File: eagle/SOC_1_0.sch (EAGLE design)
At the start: 16 parts, among them X1 A, X2 B, X3 X, X4 Y

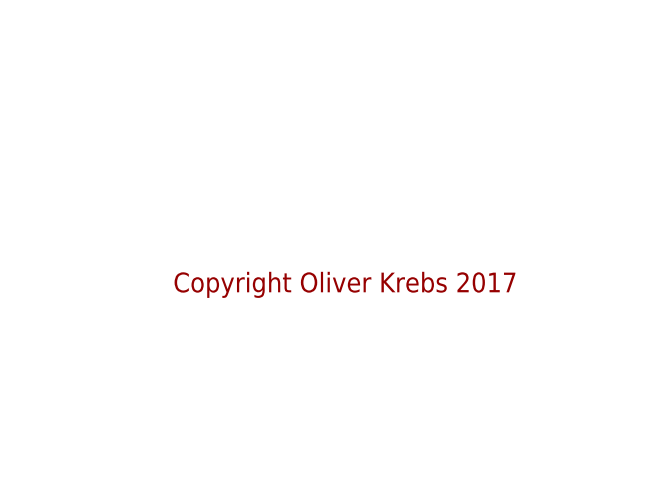
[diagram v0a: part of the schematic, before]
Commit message: New boards: eagle files (sch, brd) +ALU_1_0, CNT_1_1, D12_1_0, D14_1_0, D18_1_0, DIP_1_0, M81_1_0, N33_1_0, SWI_1_1 *SOC_1_0 modified
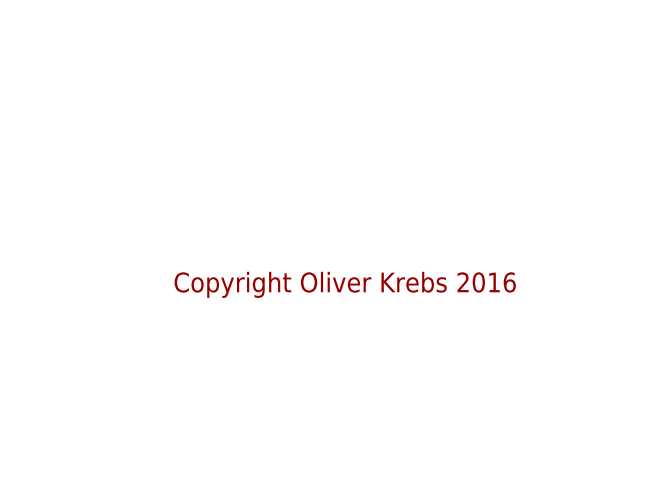
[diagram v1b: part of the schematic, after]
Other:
- note added: "Copyright Oliver Krebs 2016"
- note removed: "Copyright Oliver Krebs 2017"
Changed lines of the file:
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@@
 QUALITY AND FITNESS FOR A PARTICULAR PURPOSE.
 Please see the CERN OHL v.1.2 for applicable conditions</text>
-<text x="163.83" y="25.4" size="2.1844" layer="94">Copyright Oliver Krebs 2017</text>
+<text x="163.83" y="25.4" size="2.1844" layer="94">Copyright Oliver Krebs 2016</text>
 </plain>
 <instances>
